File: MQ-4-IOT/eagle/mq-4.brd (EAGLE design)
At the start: 100 x 80 mm, 1 part

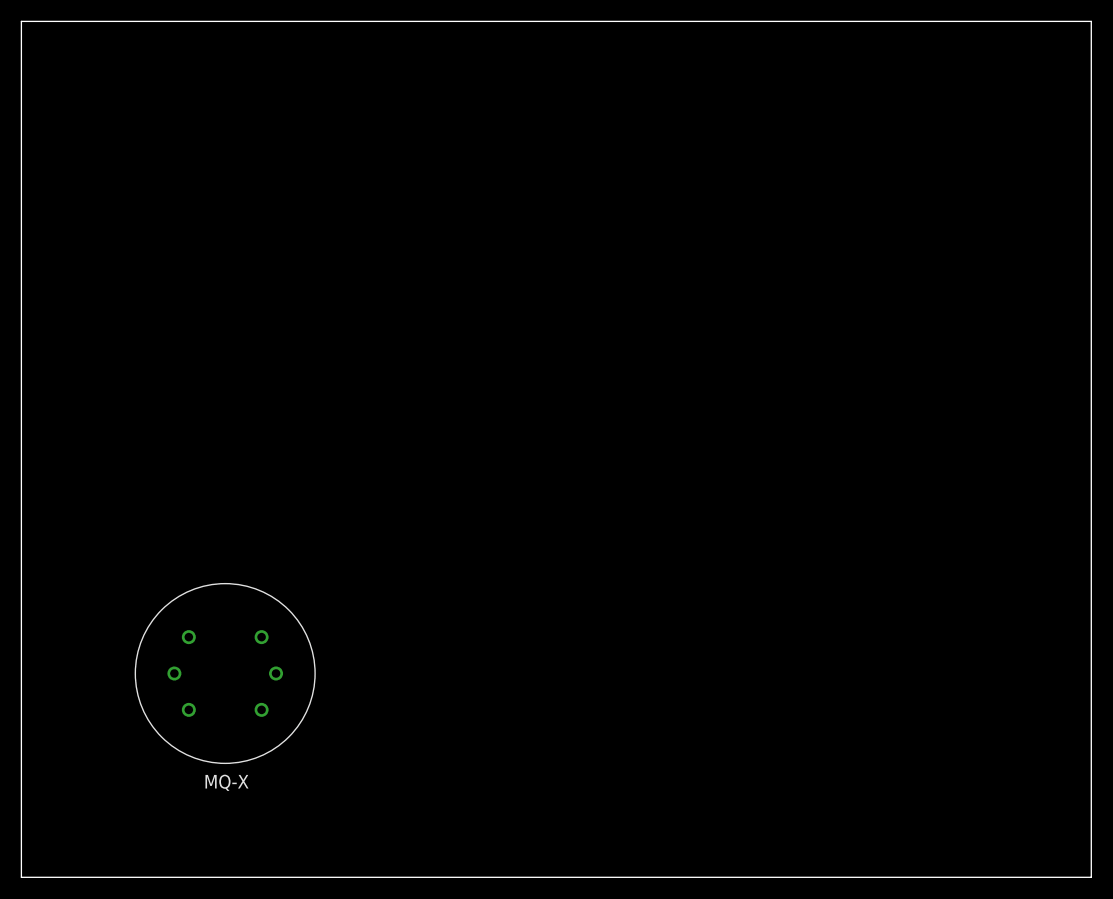
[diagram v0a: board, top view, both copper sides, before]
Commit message: MQ-4 breakout added.
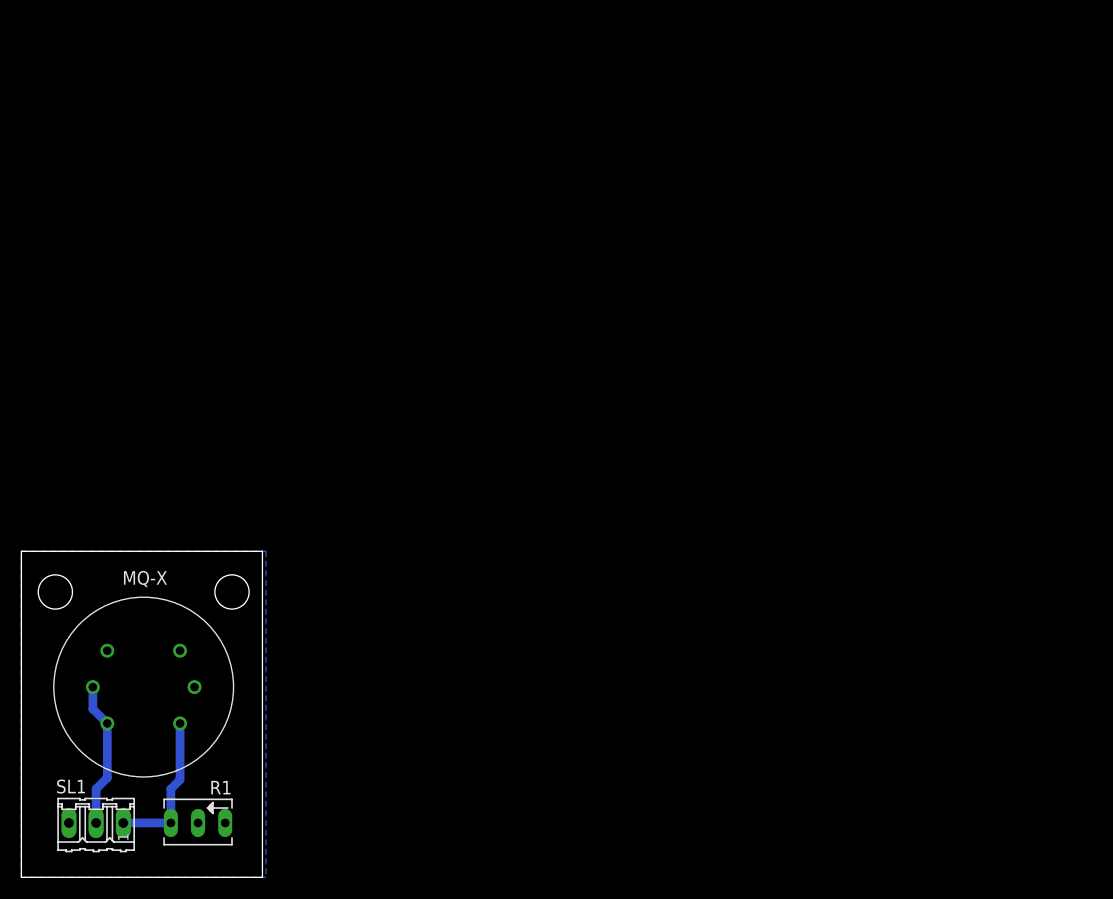
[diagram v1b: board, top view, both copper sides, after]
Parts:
- added R1: 50k, pot:B64Y
- added SL1: (no value), con-amp-quick:03P
- moved U$1 7.73 mm to (11.4, 17.8)
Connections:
- new net GND: R1.E, R1.S, SL1.3, U$1.H1
- new net VCC: SL1.2, U$1.A1, U$1.H
- new net VOUT: R1.A, SL1.1, U$1.B1
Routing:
- net VOUT: track 0.00 -> 14.1 mm
- net VCC: track 0.00 -> 13.7 mm
- added copper zone on layer 16, net GND
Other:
- board size 100 x 80 mm -> 22.5 x 30.5 mm
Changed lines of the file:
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@@
 <setting verticaltext="up"/>
 </settings>
-<grid distance="0.05" unitdist="inch" unit="inch" style="lines" multiple="1" display="no" altdistance="0.025" altunitdist="inch" altunit="inch"/>
+<grid distance="0.05" unitdist="inch" unit="inch" style="lines" multiple="1" display="yes" altdistance="0.025" altunitdist="inch" altunit="inch"/>
 <layers>
 <layer number="1" name="Top" color="4" fill="1" visible="yes" active="yes"/>
@@
 <layer number="43" name="vRestrict" color="2" fill="10" visible="yes" active="yes"/>
 <layer number="44" name="Drills" color="7" fill="1" visible="no" active="yes"/>
-<layer number="45" name="Holes" color="7" fill="1" visible="no" active="yes"/>
+<layer number="45" name="Holes" color="7" fill="1" visible="yes" active="yes"/>
 <layer number="46" name="Milling" color="3" fill="1" visible="no" active="yes"/>
 <layer number="47" name="Measures" color="7" fill="1" visible="no" active="yes"/>
@@
 <board>
 <plain>
-<wire x1="0" y1="0" x2="100" y2="0" width="0" layer="20"/>
-<wire x1="100" y1="0" x2="100" y2="80" width="0" layer="20"/>
-<wire x1="100" y1="80" x2="0" y2="80" width="0" layer="20"/>
-<wire x1="0" y1="80" x2="0" y2="0" width="0" layer="20"/>
+<wire x1="0" y1="0" x2="22.53" y2="0" width="0" layer="20"/>
+<wire x1="22.53" y1="0" x2="22.53" y2="30.47" width="0" layer="20"/>
+<wire x1="22.53" y1="30.47" x2="0" y2="30.47" width="0" layer="20"/>
+<wire x1="0" y1="30.47" x2="0" y2="0" width="0" layer="20"/>
+<hole x="3.175" y="26.67" drill="3.2"/>
+<hole x="19.685" y="26.67" drill="3.2"/>
 </plain>
 <attributes>
@@
 </variantdefs>
 <classes>
-<class number="0" name="default" width="0" drill="0">
+<class number="0" name="default" width="1.27" drill="0.6096">
+<clearance class="0" value="0.508"/>
+</class>
+<class number="1" name="gnd" width="0.9144" drill="0.254">
 </class>
 </classes>
@@
 <autorouter>
 <pass name="Default">
-<param name="RoutingGrid" value="50mil"/>
+<param name="RoutingGrid" value="6.25mil"/>
 <param name="AutoGrid" value="1"/>
 <param name="Efforts" value="0"/>
 <param name="TopRouterVariant" value="1"/>
 <param name="tpViaShape" value="round"/>
-<param name="PrefDir.1" value="a"/>
+<param name="PrefDir.1" value="0"/>
 <param name="PrefDir.2" value="0"/>
 <param name="PrefDir.3" value="0"/>
@@
 <param name="PrefDir.14" value="0"/>
 <param name="PrefDir.15" value="0"/>
-<param name="PrefDir.16" value="a"/>
+<param name="PrefDir.16" value="*"/>
 <param name="cfVia" value="8"/>
 <param name="cfNonPref" value="5"/>
@@
 </autorouter>
 <elements>
-<element name="U$1" library="mq-x" package="MQ-4" value="MQ-4" x="19.05" y="19.05"/>
+<element name="U$1" library="mq-x" package="MQ-4" value="MQ-4" x="11.43" y="17.78" smashed="yes"/>
+<element name="R1" library="pot" package="B64Y" value="50k" x="16.51" y="5.08" smashed="yes" rot="R180">
+<attribute name="NAME" x="19.685" y="9.017" size="1.27" layer="25" ratio="10" rot="R180"/>
+<attribute name="VALUE" x="15.875" y="2.54" size="1.27" layer="27" ratio="10" rot="R180"/>
+</element>
+<element name="SL1" library="con-amp-quick" package="03P" value="" x="6.985" y="5.08" smashed="yes" rot="R180">
+<attribute name="OC_NEWARK" value="unknown" x="6.985" y="5.08" size="1.778" layer="27" rot="R180" display="off"/>
+<attribute name="OC_FARNELL" value="unknown" x="6.985" y="5.08" size="1.778" layer="27" rot="R180" display="off"/>
+<attribute name="MF" value="" x="6.985" y="5.08" size="1.778" layer="27" rot="R180" display="off"/>
+<attribute name="MPN" value="" x="6.985" y="5.08" size="1.778" layer="27" rot="R180" display="off"/>
+<attribute name="NAME" x="6.096" y="9.1186" size="1.27" layer="25" ratio="10" rot="R180"/>
+<attribute name="VALUE" x="10.541" y="8.9154" size="1.27" layer="27" ratio="10" rot="R180"/>
+</element>
 </elements>
 <signals>
+<signal name="VCC">
+<contactref element="U$1" pad="H"/>
+<contactref element="U$1" pad="A1"/>
+<contactref element="SL1" pad="2"/>
+<wire x1="6.68" y1="17.78" x2="6.68" y2="15.73" width="0.8128" layer="16"/>
+<wire x1="6.68" y1="15.73" x2="8.03" y2="14.38" width="0.8128" layer="16"/>
+<wire x1="8.03" y1="14.38" x2="8.03" y2="9.3" width="0.8128" layer="16"/>
+<wire x1="8.03" y1="9.3" x2="6.985" y2="8.255" width="0.8128" layer="16"/>
+<wire x1="6.985" y1="8.255" x2="6.985" y2="5.08" width="0.8128" layer="16"/>
+</signal>
+<signal name="GND" class="1">
+<contactref element="R1" pad="E"/>
+<contactref element="R1" pad="S"/>
+<contactref element="U$1" pad="H1"/>
+<contactref element="SL1" pad="3"/>
+<polygon width="0.4064" layer="16">
+<vertex x="0" y="0"/>
+<vertex x="0" y="30.48"/>
+<vertex x="22.86" y="30.48"/>
+<vertex x="22.86" y="0"/>
+</polygon>
+</signal>
+<signal name="VOUT">
+<contactref element="SL1" pad="1"/>
+<contactref element="U$1" pad="B1"/>
+<contactref element="R1" pad="A"/>
+<wire x1="14.83" y1="14.38" x2="14.83" y2="9.115" width="0.8128" layer="16"/>
+<wire x1="14.83" y1="9.115" x2="13.97" y2="8.255" width="0.8128" layer="16"/>
+<wire x1="13.97" y1="8.255" x2="13.97" y2="5.08" width="0.8128" layer="16"/>
+<wire x1="13.97" y1="5.08" x2="9.525" y2="5.08" width="0.8128" layer="16"/>
+</signal>
 </signals>
 </board>
